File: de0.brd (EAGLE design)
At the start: 150.3 x 98.4 mm, 154 parts, among them IC1 PL2303SA__LF, J2 UX60SC-MB-5ST, Q1 BSH103,235, Q2 BSH103,235, Q3 BSH103,235, Q4 BSH103,235, Q5 BSH103,235, SW0 SS12SDP2, SW1 SS12SDP2, SW2 SS12SDP2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

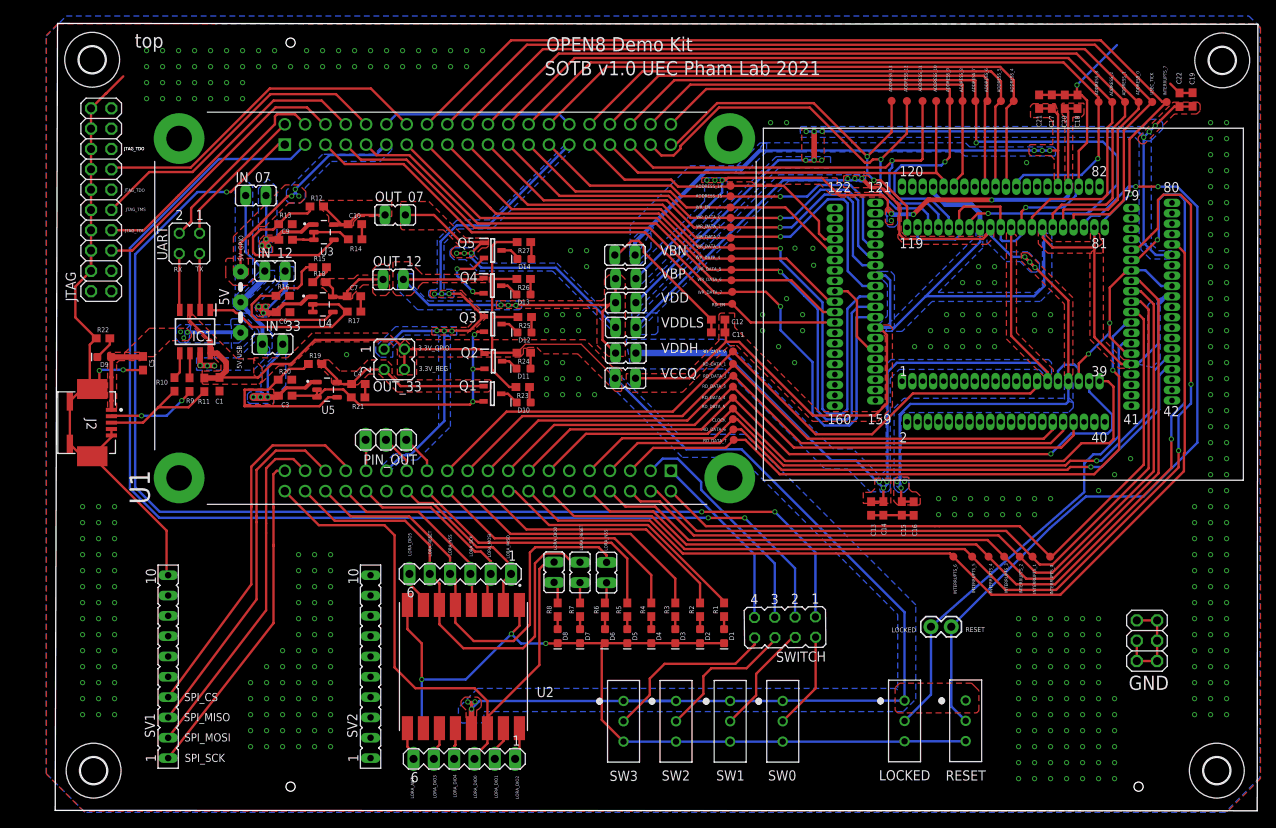
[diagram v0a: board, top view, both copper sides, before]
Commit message: change USB connector
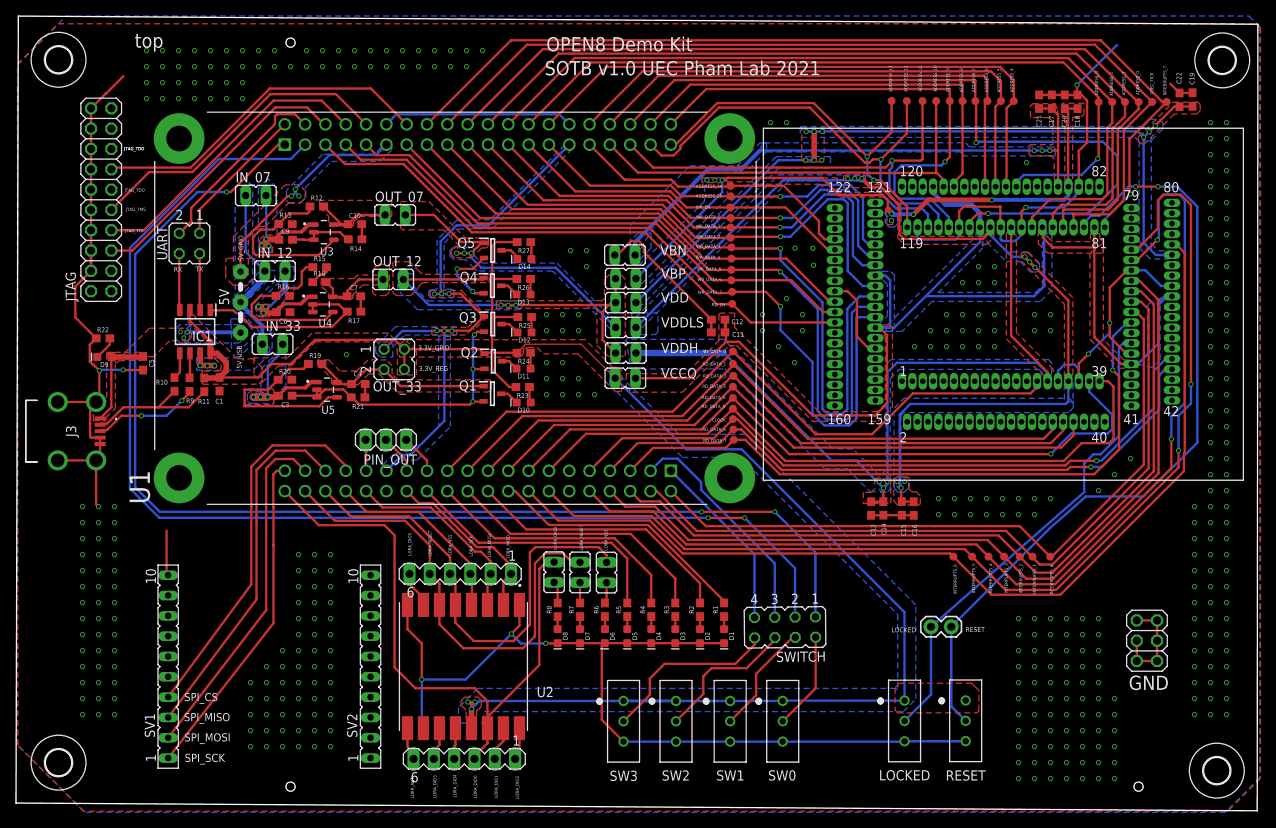
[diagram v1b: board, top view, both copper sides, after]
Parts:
- removed J2: UX60SC-MB-5ST, Connector_USB:UX60SC-MB-5ST
- added J3: U-M-M5DD-W-1, SamacSys_Parts:UMM5DDW1
- moved H2 4.49 mm to (-65.0, -37.0)
- moved H1 4.20 mm to (-65.0, 50.9)
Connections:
- net D+: now also J3.2; no longer J2.3
- net D-: now also J3.3; no longer J2.2
- net GND: now also J3.4, J3.5, J3.MH1, J3.MH2, J3.MH3, J3.MH4; no longer J2.4, J2.5, J2.6, J2.7, J2.8, J2.9
- net VDD5_USB: now also J3.1; no longer J2.1
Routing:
- net GND: track 457.3 -> 449.9 mm
- net D-: track 11.1 -> 13.3 mm
- net VDD5_USB: track 17.3 -> 18.9 mm
- net D+: track 16.1 -> 17.6 mm
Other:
- board size 150.3 x 98.4 mm -> 155.2 x 99.3 mm
